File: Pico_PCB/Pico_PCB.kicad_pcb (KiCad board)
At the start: 2 copper layers, 71 parts, among them J1 USB_A, J4 Conn_02x04_Counter_Clockwise, SW1 SPST_Momentary_4.6x2.8mm, SW2 SPST_Momentary_4.6x2.8mm, U1 AT90USB647-A, Y1 Crystal_GND24

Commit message: PCB_03/09
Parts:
- added C1: 4.7 uF, Capacitor_SMD:C_0603_1608Metric_Pad1.08x0.95mm_HandSolder, F.Cu at (183.0, 85.8)
- added TP35: TestPoint, TestPoint:TestPoint_THTPad_D1.5mm_Drill0.7mm, F.Cu at (198.3, 86.5)
- C11: value 100nF -> 4.7 uF
- moved R4 69.2 mm to (199.6, 66.1)
- moved C9 65.3 mm to (190.1, 64.3), turned to 90 degrees
- moved R14 58.8 mm to (203.0, 75.5)
- moved SW2 57.4 mm to (204.8, 71.4), turned to 180 degrees
- moved R9 56.7 mm to (203.0, 84.0)
- moved R13 55.9 mm to (203.0, 77.2)
- moved C10 54.8 mm to (173.3, 68.2), turned to 90 degrees
- moved R8 54.3 mm to (203.0, 85.7)
- moved R12 53.2 mm to (203.0, 78.8)
- moved R11 50.7 mm to (203.0, 80.5)
- moved R5 50.1 mm to (203.0, 87.4)
- moved R10 48.5 mm to (203.0, 82.2)
- moved C11 48.1 mm to (177.3, 65.7), turned to 180 degrees
- moved D6 45.4 mm to (206.8, 84.0), turned to 180 degrees
- moved D11 44.4 mm to (206.8, 75.5), turned to 180 degrees
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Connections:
- TP1 pad 1: +5V -> Net-(U1-PA0)
- TP28 pad 1: +5V -> Net-(U1-PE7)
- U1 pad 2: +5V -> Net-(U1-PE7)
- U1 pad 34: unconnected-(U1-PE1-Pad34) -> Net-(U1-PE1)
- U1 pad 51: +5V -> Net-(U1-PA0)
- U1 pad 53: +5V -> GND
- U1 pad 63: +5V -> GND
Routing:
- net +5V: track 30.0 -> 102.4 mm
- net INT: track 0.00 -> 33.2 mm
- net RESET: track 0.00 -> 32.2 mm, vias 0 -> 1
- net MOSI: track 0.00 -> 27.2 mm
- net SS: track 0.00 -> 19.7 mm
- net HWB: track 0.00 -> 17.7 mm
- net MISO: track 0.00 -> 17.4 mm
- net SCK: track 0.00 -> 17.0 mm
- net Net-(U1-XTAL1): track 0.00 -> 15.4 mm
- net TEST0: track 0.00 -> 12.5 mm
- net Net-(U1-PE7): track 0.00 -> 11.8 mm
- net TEST1: track 0.00 -> 11.5 mm
- net TEST2: track 0.00 -> 11.1 mm
- net TEST3: track 0.00 -> 10.7 mm
- net Net-(U1-XTAL2): track 0.00 -> 10.5 mm
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- added copper zone on B.Cu, net GND
- added copper zone on F.Cu, net GND
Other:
- board outline added: 60.1 x 41.9 mm

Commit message: PCB_fini
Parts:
- removed TP12: TestPoint, TestPoint:TestPoint_THTPad_D1.5mm_Drill0.7mm
- C1: value 4.7 uF -> 1uF
- C10: value 100nF -> 1uF
- C11: value 4.7 uF -> 100nF
- C9: value 4.7uF -> 100nF
- moved TP23 89.8 mm to (271.1, 43.7)
- moved TP16 87.5 mm to (268.1, 45.0)
- moved TP14 87.5 mm to (265.3, 45.0)
- moved C7 87.3 mm to (261.8, 48.8)
- moved TP35 86.6 mm to (272.2, 41.3)
- moved TP6 86.4 mm to (270.5, 25.9)
- moved Y1 86.4 mm to (258.1, 47.9), turned to 180 degrees
- moved TP18 86.4 mm to (270.6, 46.8)
- moved TP4 86.2 mm to (270.2, 23.1)
- moved TP5 86.2 mm to (272.5, 24.4)
- moved TP8 86.2 mm to (270.3, 28.8)
- moved TP7 86.1 mm to (272.6, 27.5)
- moved C3 85.8 mm to (246.5, 30.0)
- moved R13 85.8 mm to (276.5, 33.0)
- moved R14 85.8 mm to (276.5, 31.2)
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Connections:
- U1 pad 25: Net-(U1-PD0) -> unconnected-(U1-PD0-Pad25)
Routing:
- net Net-(U1-PD0): track 10.5 -> 0.00 mm
- net +5V: track 102.4 -> 111.3 mm
- net Net-(U1-XTAL2): track 10.5 -> 17.6 mm
- net INT: track 33.2 -> 28.0 mm
- net Net-(U1-PE0): track 12.6 -> 8.38 mm
- net GND: track 8.73 -> 4.53 mm, vias 2 -> 45
- net Net-(U1-PD6): track 8.95 -> 12.0 mm
- net Net-(U1-XTAL1): track 15.4 -> 13.4 mm
- net RESET: track 32.2 -> 30.2 mm
- net Net-(U1-PD4): track 7.55 -> 9.39 mm
- net Net-(U1-PD1): track 12.3 -> 11.3 mm
- net Net-(U1-PD7): track 6.30 -> 5.27 mm
- net Net-(U1-PD2): track 7.06 -> 7.94 mm
- net 3.3V: track 4.71 -> 5.37 mm
- net Net-(U1-PA5): track 3.15 -> 3.79 mm
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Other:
- board size 60.1 x 41.9 mm -> 52.6 x 42 mm
- board text added: "Romain DUHR Louis DERYCKERE Christian CLAVIER"

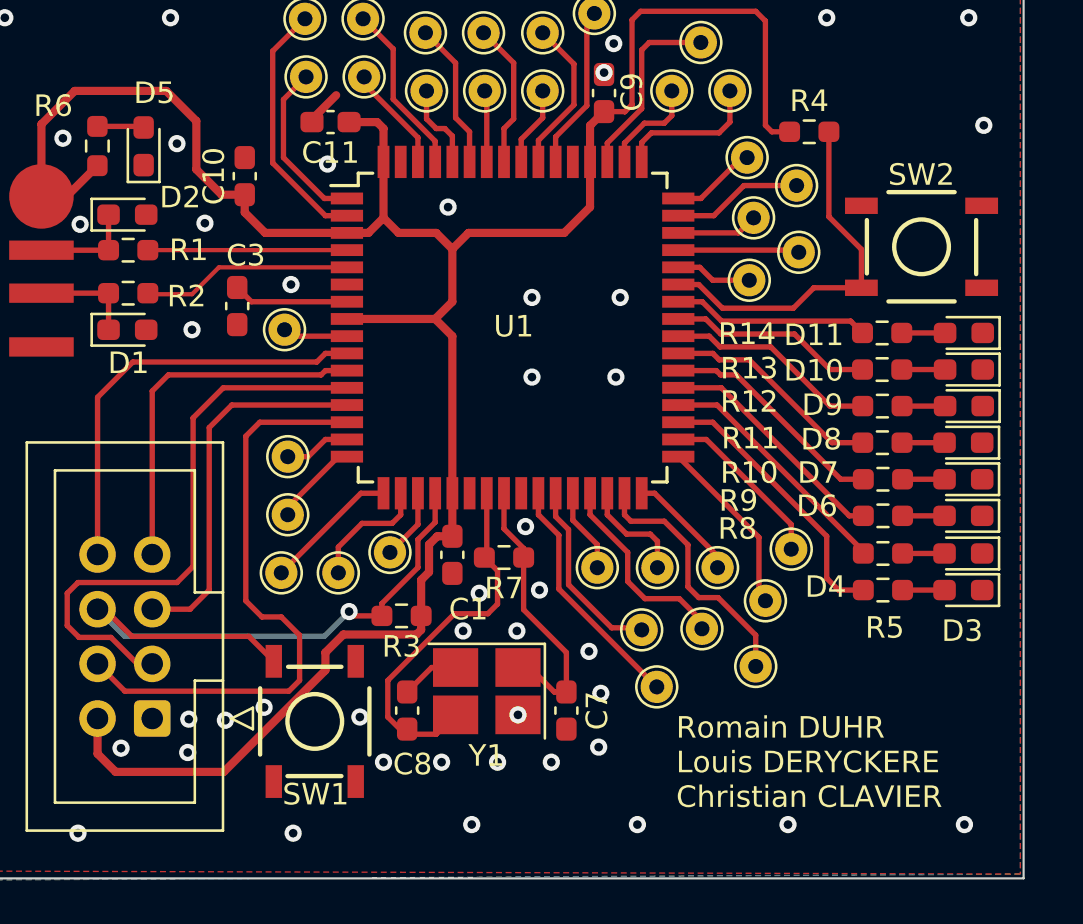
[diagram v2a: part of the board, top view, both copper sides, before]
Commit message: Modif PCB boutons
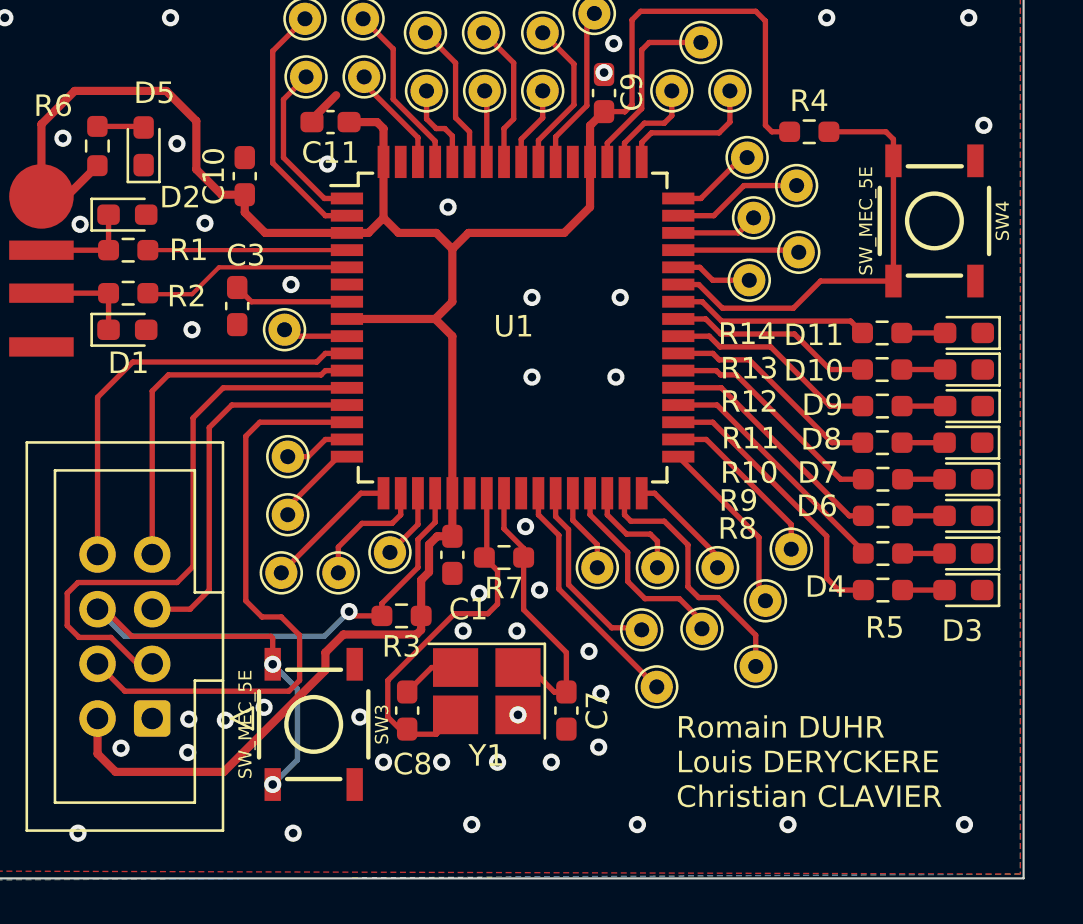
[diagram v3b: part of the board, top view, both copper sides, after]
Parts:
- removed SW1, SW2: SPST_Momentary_4.6x2.8mm, Switches:TACTILE_SWITCH_SMD_5.2MM
- added SW3: SW_MEC_5E, Spark-Switches:TACTILE_SWITCH_SMD_5.2MM, F.Cu at (250.1, 49.4)
- added SW4: SW_MEC_5E, Spark-Switches:TACTILE_SWITCH_SMD_5.2MM, F.Cu at (278.9, 26.0)
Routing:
- net RESET: track 30.2 -> 37.5 mm, vias 1 -> 3
- net HWB: track 17.2 -> 20.7 mm
